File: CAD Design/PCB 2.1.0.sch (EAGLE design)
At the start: 55 parts, among them U1 CC2538, U2 MAX1555, X1 32MHz, X2 FC-12M

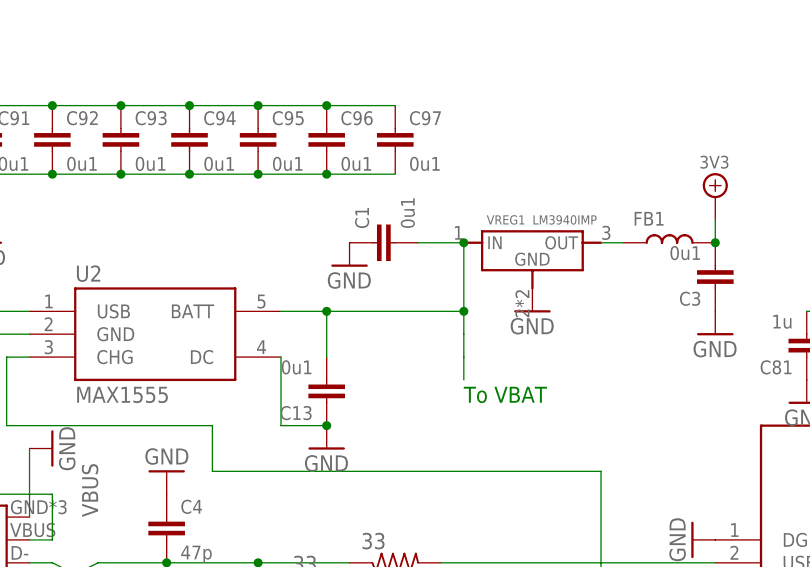
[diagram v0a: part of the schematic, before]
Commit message: Schematic Update, board push
Replaced some capacitors, 2.1 board with preliminary element placement
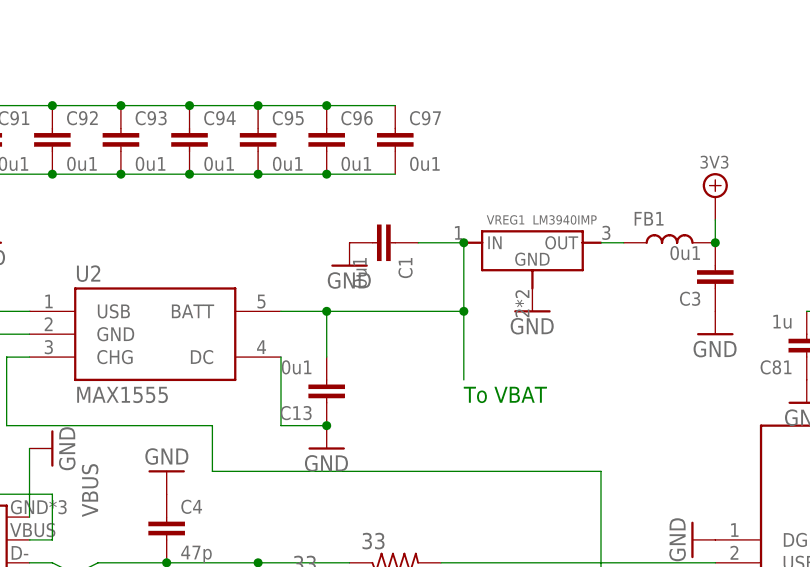
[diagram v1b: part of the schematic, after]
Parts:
- C1, C13, C3: device discrete:CC1206 -> discrete:CC0402
- C5: device discrete:CC0603 -> discrete:CC0402
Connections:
- net GND: now also C1.2; no longer C1.1
- net N$14: now also C1.1; no longer C1.2
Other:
- moved on the sheet: C1
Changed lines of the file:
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@@
 <part name="3V3_PWR4" library="supply" deviceset="3V3" device=""/>
 <part name="GND17" library="supply1" deviceset="GND" device=""/>
-<part name="C1" library="discrete" deviceset="C" device="C1206" value="0u1"/>
 <part name="GND18" library="supply1" deviceset="GND" device=""/>
 <part name="LED2" library="discrete" deviceset="LED" device="805"/>
-<part name="C3" library="discrete" deviceset="C" device="C1206" value="0u1"/>
 <part name="GND4" library="supply1" deviceset="GND" device=""/>
 <part name="U1" library="ic" deviceset="CC2538" device=""/>
@@
 <part name="C94" library="discrete" deviceset="C" device="C0402" value="0u1"/>
 <part name="VREG1" library="voltage-regulators" deviceset="LM3940" device="IMP"/>
-<part name="C5" library="discrete" deviceset="C" device="C0603" value="1n"/>
 <part name="GND9" library="supply1" deviceset="GND" device=""/>
 <part name="X2" library="crystal" deviceset="FC-12M" device=""/>
@@
 <part name="C12" library="discrete" deviceset="C" device="C0603" value="47p"/>
 <part name="GND36" library="supply1" deviceset="GND" device=""/>
-<part name="C13" library="discrete" deviceset="C" device="C1206" value="0u1"/>
 <part name="GND37" library="supply1" deviceset="GND" device=""/>
 <part name="RESET" library="SparkFun-Electromechanical" deviceset="TAC_SWITCH" device="SMD"/>
@@
 <part name="R3" library="rcl" deviceset="R-US_" device="R0402" value="33"/>
 <part name="R5" library="rcl" deviceset="R-US_" device="R0402" value="2k2"/>
+<part name="C3" library="discrete" deviceset="C" device="C0402" value="0u1"/>
+<part name="C13" library="discrete" deviceset="C" device="C0402" value="0u1"/>
+<part name="C1" library="discrete" deviceset="C" device="C0402" value="0u1"/>
+<part name="C5" library="discrete" deviceset="C" device="C0402" value="1n"/>
 </parts>
 <sheets>
@@
 <instance part="3V3_PWR4" gate="A" x="96.52" y="152.4"/>
 <instance part="GND17" gate="1" x="76.2" y="139.7"/>
-<instance part="C1" gate="C" x="58.42" y="147.32" rot="R90"/>
 <instance part="GND18" gate="1" x="167.64" y="132.08"/>
 <instance part="LED2" gate="LED" x="50.8" y="91.44"/>
-<instance part="C3" gate="C" x="96.52" y="142.24" rot="R180"/>
 <instance part="GND4" gate="1" x="96.52" y="137.16"/>
 <instance part="U1" gate="G$1" x="129.54" y="99.06"/>
@@
 <instance part="C94" gate="C" x="38.1" y="160.02"/>
 <instance part="VREG1" gate="A" x="76.2" y="142.24"/>
-<instance part="C5" gate="C" x="152.4" y="53.34" rot="R270"/>
 <instance part="GND9" gate="1" x="157.48" y="53.34" rot="R90"/>
 <instance part="X2" gate="G$1" x="205.74" y="154.94"/>
@@
 <instance part="C12" gate="C" x="10.16" y="134.62"/>
 <instance part="GND36" gate="1" x="10.16" y="124.46"/>
-<instance part="C13" gate="C" x="53.34" y="129.54" rot="R180"/>
 <instance part="GND37" gate="1" x="53.34" y="124.46"/>
 <instance part="RESET" gate="S" x="170.18" y="55.88" rot="R180"/>
@@
 <instance part="R3" gate="G$1" x="53.34" y="109.22" rot="MR180"/>
 <instance part="R5" gate="G$1" x="152.4" y="60.96" rot="MR180"/>
+<instance part="C3" gate="C" x="96.52" y="142.24" rot="R180"/>
+<instance part="C13" gate="C" x="53.34" y="129.54" rot="R180"/>
+<instance part="C1" gate="C" x="60.96" y="147.32" rot="R270"/>
+<instance part="C5" gate="C" x="152.4" y="53.34" rot="R270"/>
 </instances>
 <busses>
@@
 <wire x1="167.64" y1="137.16" x2="167.64" y2="134.62" width="0.1524" layer="91"/>
 <pinref part="JTAG" gate="-GND" pin="S"/>
-</segment>
-<segment>
-<pinref part="C3" gate="C" pin="1"/>
-<pinref part="GND4" gate="1" pin="GND"/>
 </segment>
 <segment>
@@
 </segment>
 <segment>
-<pinref part="C1" gate="C" pin="1"/>
-<pinref part="GND26" gate="1" pin="GND"/>
-</segment>
-<segment>
 <pinref part="B1" gate="G$1" pin="5"/>
 <wire x1="220.98" y1="116.84" x2="213.36" y2="116.84" width="0.1524" layer="91"/>
@@
 </segment>
 <segment>
-<pinref part="C5" gate="C" pin="1"/>
-<pinref part="GND9" gate="1" pin="GND"/>
-</segment>
-<segment>
 <pinref part="U1" gate="G$1" pin="DGND_USB"/>
 <pinref part="GND29" gate="1" pin="GND"/>
@@
 </segment>
 <segment>
-<pinref part="C13" gate="C" pin="1"/>
 <pinref part="GND37" gate="1" pin="GND"/>
 <pinref part="U2" gate="G$1" pin="DC"/>
 <wire x1="48.26" y1="134.62" x2="48.26" y2="127" width="0.1524" layer="91"/>
 <wire x1="48.26" y1="127" x2="53.34" y2="127" width="0.1524" layer="91"/>
+<pinref part="C13" gate="C" pin="1"/>
 <junction x="53.34" y="127"/>
 </segment>
@@
 <junction x="99.06" y="55.88"/>
 <pinref part="GND39" gate="1" pin="GND"/>
+</segment>
+<segment>
+<pinref part="GND4" gate="1" pin="GND"/>
+<pinref part="C3" gate="C" pin="1"/>
+</segment>
+<segment>
+<pinref part="GND26" gate="1" pin="GND"/>
+<pinref part="C1" gate="C" pin="2"/>
+</segment>
+<segment>
+<pinref part="GND9" gate="1" pin="GND"/>
+<pinref part="C5" gate="C" pin="1"/>
 </segment>
 </net>
@@
 <segment>
 <pinref part="FB1" gate="L" pin="P$2"/>
-<pinref part="C3" gate="C" pin="2"/>
 <pinref part="3V3_PWR4" gate="A" pin="3V3"/>
 <wire x1="96.52" y1="149.86" x2="96.52" y2="147.32" width="0.1524" layer="91"/>
+<pinref part="C3" gate="C" pin="2"/>
 <junction x="96.52" y="147.32"/>
 </segment>
@@
 <segment>
 <pinref part="U1" gate="G$1" pin="RESET_N"/>
-<pinref part="C5" gate="C" pin="2"/>
 <wire x1="147.32" y1="63.5" x2="147.32" y2="60.96" width="0.1524" layer="91"/>
 <pinref part="RESET" gate="S" pin="4"/>
@@
 <pinref part="R5" gate="G$1" pin="1"/>
 <junction x="147.32" y="60.96"/>
+<pinref part="C5" gate="C" pin="2"/>
 </segment>
 </net>
@@
 <segment>
 <pinref part="U2" gate="G$1" pin="BATT"/>
-<pinref part="C1" gate="C" pin="2"/>
 <pinref part="VREG1" gate="A" pin="IN"/>
 <wire x1="68.58" y1="147.32" x2="63.5" y2="147.32" width="0.1524" layer="91"/>
@@
 <junction x="68.58" y="147.32"/>
 <wire x1="53.34" y1="139.7" x2="53.34" y2="134.62" width="0.1524" layer="91"/>
-<pinref part="C13" gate="C" pin="2"/>
 <junction x="53.34" y="139.7"/>
 <junction x="68.58" y="139.7"/>
-<wire x1="68.58" y1="134.62" x2="68.58" y2="137.16" width="0.1524" layer="91"/>
-<wire x1="68.58" y1="137.16" x2="68.58" y2="139.7" width="0.1524" layer="91"/>
-<wire x1="68.58" y1="134.62" x2="68.58" y2="132.08" width="0.1524" layer="91"/>
-</segment>
-</net>
+<wire x1="68.58" y1="139.7" x2="68.58" y2="132.08" width="0.1524" layer="91"/>
+<pinref part="C13" gate="C" pin="2"/>
+<pinref part="C1" gate="C" pin="1"/>
+</segment>
+</net>
